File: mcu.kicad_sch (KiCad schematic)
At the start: 38 parts, among them Q4 MMBT3904, U2 AT32F403ACGT7, U3 QMI8658B, Y1 8MHz, Y2 32.768kHz

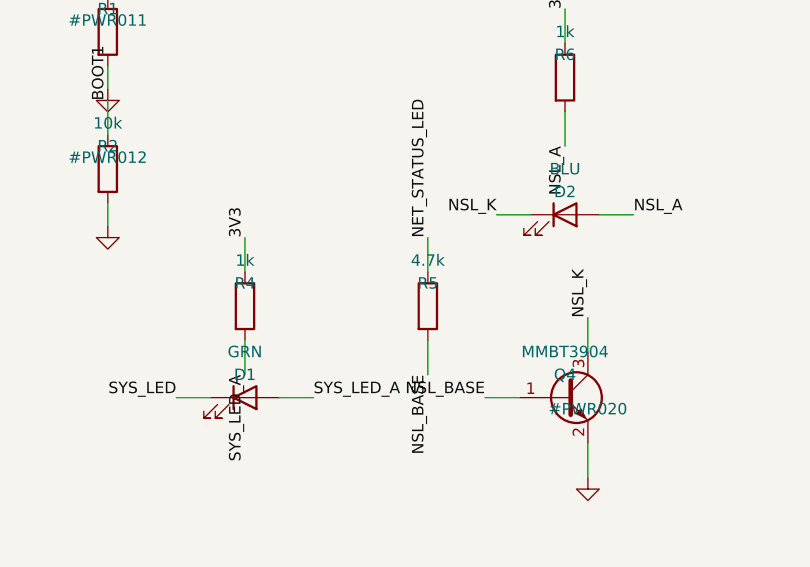
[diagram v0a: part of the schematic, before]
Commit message: M2: modem_rf ERC-clean (F-9 conditional release)
EC200U wired using ONLY Table-7-VERIFIED pins; all 76 NEEDS-HUMAN pins are
no-connect with F9-REVIEW text markers on the sheet. VBAT (57-60) via Q3
AO3401A high-side switch (DEFAULT ON, MODEM_PWR_EN high = power cut via
Q14 NPN + Q13 PNP); PWRKEY/RESET_N NPN open-collector stages; STATUS per
Quectel Fig 28 NPN stage (MODEM_STATUS INVERTED at MCU - firmware note);
UART/RI/DTR through TXB0104PWR (VccA=VDD_EXT 1.8V, OE held low until
VDD_EXT rises); USIM with 33R series + SMF05C + nano holder + MFF2 eSIM
pads DNP behind 0R selects; USB to 4 test pads via USBLC6-2SC6; NETLIGHT
NPN LED; pi networks (0R fitted, shunts DNP) to 2x XY-IPEX1 U.FL.

Root-sheet layout bug fixed: a 5th sheet wrapped onto column 0 and its
pin stubs shorted into the mcu sheet's stubs (5V0/ADC_SPARE, CAN1_RX/SYS,
CAN1_TX/VIN) - rows added. USIM_VDD 0R select was defeated by a label
bridge - holder now on USIM_VDD_SIM only.

Co-Authored-By: Claude Fable 5 <noreply@anthropic.com>
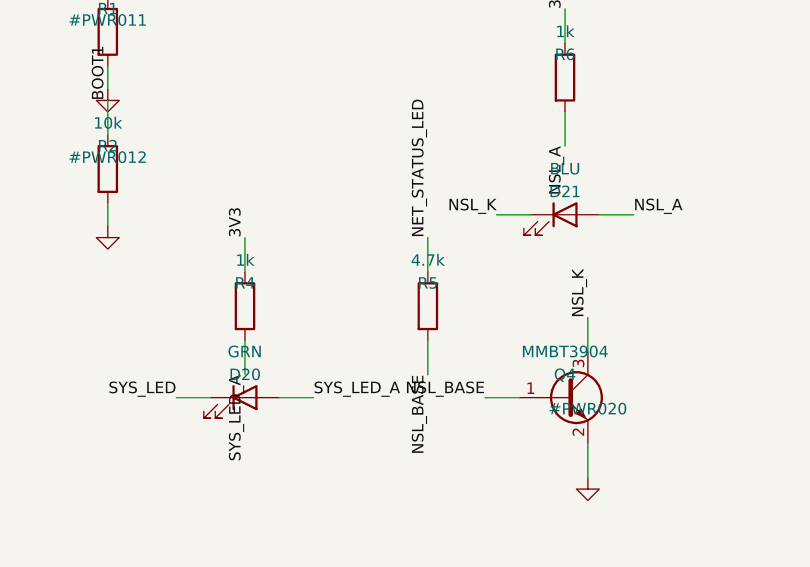
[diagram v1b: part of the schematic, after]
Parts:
- removed D1: GRN, LED_SMD:LED_0603_1608Metric, symbol Device:LED
- removed D2: BLU, LED_SMD:LED_0603_1608Metric, symbol Device:LED
- added D20: GRN, LED_SMD:LED_0603_1608Metric, symbol Device:LED
- added D21: BLU, LED_SMD:LED_0603_1608Metric, symbol Device:LED
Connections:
- net NSL_A: now also D21.2 (A)
- net NSL_K: now also D21.1 (K)
- net SYS_LED: now also D20.1 (K)
- net SYS_LED_A: now also D20.2 (A)
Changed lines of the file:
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@@
 		(dnp no)
 		(fields_autoplaced yes)
-		(property "Reference" "D1"
+		(property "Reference" "D20"
 			(at 320.04 198.12 0)
 			(effects
@@
 			(project "telematics-tracker"
 				(path "/784bc421-9fc7-43cb-bfc3-562714cb3f68/f6e9097b-45bc-5b1a-80f4-03a0e0f8043a"
-					(reference "D1")
+					(reference "D20")
 					(unit 1)
 				)
@@
 		(dnp no)
 		(fields_autoplaced yes)
-		(property "Reference" "D2"
+		(property "Reference" "D21"
 			(at 355.6 177.8 0)
 			(effects
@@
 			(project "telematics-tracker"
 				(path "/784bc421-9fc7-43cb-bfc3-562714cb3f68/f6e9097b-45bc-5b1a-80f4-03a0e0f8043a"
-					(reference "D2")
-					(unit 1)
-				)
+					(reference "D21")
+					(unit 1)
+				)

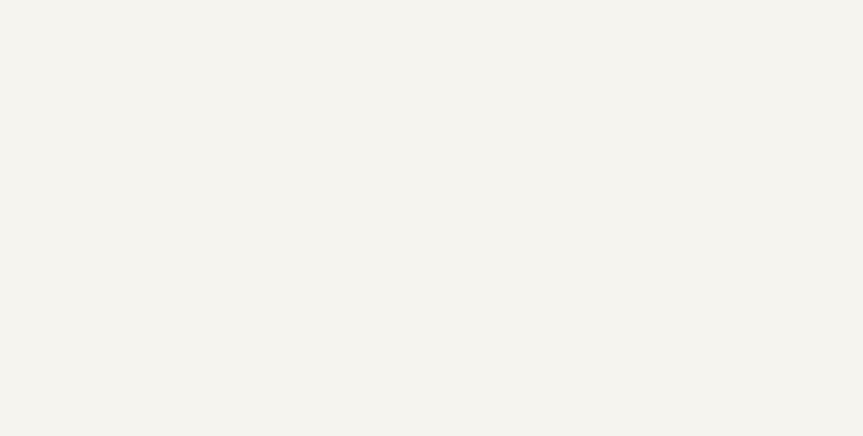
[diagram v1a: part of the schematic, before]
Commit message: M3 close: F-15 R80 1R, F-14 six test points, ambient rating, CPWG geometry
F-15: R80 10R (C3013385) -> 1R anti-surge FRS2512F1R00TS (C55348540).
At the 10.5 V floor and full load the 10R version had NO load-line solution:
V_B^2 - 9.8*V_B + 59 = 0, discriminant -140. Max power transfer through 10R
from 9.8 V is V^2/4R = 2.4 W against a 5.9 W demand - a hard brown-out. At 1R:
V_B = 9.16 V, I = 0.644 A, 0.41 W worst-case continuous, 24 W ceiling.
Pulse energy unchanged at 8.5 mJ (E = CdV^2/2 is independent of R) but peak
goes 384 W -> 3.8 kW and tau 44 us -> 4.4 us, which is why the part must be
anti-surge rather than plain thick film. Confirming that pulse curve joins F-12
on the bench list.

F-14: TP23 VIN, TP24 VBAT_MODEM, TP25 CANH, TP26 CANL, TP27 MODEM_TX,
TP28 MODEM_RX. Each verified against the netlist to share its net with the
real circuit nodes. hier() used for hierarchical nets and net() only for
sheet-local ones, so ERC stayed at exactly 0 errors / 14 warnings with no new
same_local_global_label entries. Rule 8 now MET (28 test points).

Product spec: rated operating ambient -20 to +70 C, housing shaded or
light-coloured, 85 C survival not operating - added to handoff section 1.1 and
a new docs/installation-sheet.md. Governed by U1: EC200U V1.2 Table 42 p.75
gives operating -35..+75 C (meets 3GPP) and extended -40..+85 C (functions
maintained but Pout may exceed 3GPP tolerances), so +70 C keeps 5 C to the
compliant limit and 85 C is exactly the extended limit.

NEW FLAG F-19: typical 1S Li-ion is -20..+60 C discharge, narrower than the
+70 C product ceiling. Charging is already protected by the BQ25606 JEITA
network; discharge above 60 C and calendar ageing are not. Decision needed -
accept with a shorter battery service interval, or narrow the rating to +60 C.

M4 input: 50 ohm CPWG for JLC7628 L1-L2 computed via Ghione-Naldi conformal
mapping (elliptic integrals by AGM), cross-checked against Hammerstad-Jensen
microstrip. h = 0.2104 mm (1x 7628 prepreg). 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
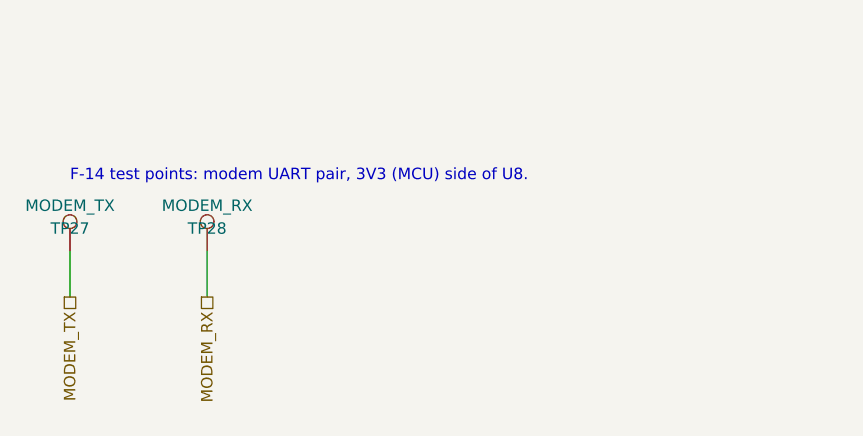
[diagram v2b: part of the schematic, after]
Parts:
- added TP27: MODEM_TX, TestPoint:TestPoint_Pad_D1.5mm, symbol Connector:TestPoint
- added TP28: MODEM_RX, TestPoint:TestPoint_Pad_D1.5mm, symbol Connector:TestPoint
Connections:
- net MODEM_RX: now also TP28.1
- net MODEM_TX: now also TP27.1
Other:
- note added: "F-14 test points: modem UART pair, 3V3 (MCU) side of U8."
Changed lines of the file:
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@@
 	(wire
 		(pts
+			(xy 30.48 271.78) (xy 30.48 276.86)
+		)
+		(stroke
+			(width 0)
+			(type default)
+		)
+	)
+	(hierarchical_label "MODEM_TX"
+		(shape passive)
+		(at 30.48 276.86 270)
+		(effects
+			(font
+				(size 1.27 1.27)
+			)
+			(justify right)
+		)
+	)
+	(wire
+		(pts
+			(xy 45.72 271.78) (xy 45.72 276.86)
+		)
+		(stroke
+			(width 0)
+			(type default)
+		)
+	)
+	(hierarchical_label "MODEM_RX"
+		(shape passive)
+		(at 45.72 276.86 270)
+		(effects
+			(font
+				(size 1.27 1.27)
+			)
+			(justify right)
+		)
+	)
+	(text "F-14 test points: modem UART pair, 3V3 (MCU) side of U8."
+		(exclude_from_sim no)
+		(at 30.48 264.16 0)
+		(effects
+			(font
+				(size 1.27 1.27)
+			)
+			(justify left bottom)
+		)
+	)
+	(wire
+		(pts
 			(xy 38.1 215.9) (xy 38.1 220.98)
 		)
@@
 					(unit 1)
 				)
+			)
+		)
+	)
+	(symbol
+		(lib_id "Connector:TestPoint")
+		(at 30.48 271.78 0)
+		(unit 1)
+		(exclude_from_sim no)
+		(in_bom yes)
+		(on_board yes)
+		(dnp no)
+		(fields_autoplaced yes)
+		(property "Reference" "TP27"
+			(at 30.48 269.24 0)
+			(effects
+				(font
+					(size 1.27 1.27)
+				)
+			)
+		)
+		(property "Value" "MODEM_TX"
+			(at 30.48 266.7 0)
+			(effects
+				(font
+					(size 1.27 1.27)
+				)
+			)
+		)
+		(property "Footprint" "TestPoint:TestPoint_Pad_D1.5mm"
+			(at 30.48 271.78 0)
+			(hide yes)
+			(effects
+				(font
+					(size 1.27 1.27)
+				)
+			)
+		)
+		(property "Datasheet" "~"
+			(at 30.48 271.78 0)
+			(hide yes)
+			(effects
+				(font
+					(size 1.27 1.27)
+				)
+			)
+		)
+		(pin "1"
+		)
+		(instances
+			(project "telematics-tracker"
+				(path "/784bc421-9fc7-43cb-bfc3-562714cb3f68/f6e9097b-45bc-5b1a-80f4-03a0e0f8043a"
+					(reference "TP27")
+					(unit 1)
+				)
+			)
+		)
+	)
+	(symbol
+		(lib_id "Connector:TestPoint")
+		(at 45.72 271.78 0)
+		(unit 1)
+		(exclude_from_sim no)
+		(in_bom yes)
+		(on_board yes)
+		(dnp no)
+		(fields_autoplaced yes)
+		(property "Reference" "TP28"
+			(at 45.72 269.24 0)
+			(effects
+				(font
+					(size 1.27 1.27)
+				)
+			)
+		)
+		(property "Value" "MODEM_RX"
+			(at 45.72 266.7 0)
+			(effects
+				(font
+					(size 1.27 1.27)
+				)
+			)
+		)
+		(property "Footprint" "TestPoint:TestPoint_Pad_D1.5mm"
+			(at 45.72 271.78 0)
+			(hide yes)
+			(effects
+				(font
+					(size 1.27 1.27)
+				)
+			)
+		)
+		(property "Datasheet" "~"
+			(at 45.72 271.78 0)
+			(hide yes)
+			(effects
+				(font
+					(size 1.27 1.27)
+				)
+			)
+		)
+		(pin "1"
+		)
+		(instances
+			(project "telematics-tracker"
+				(path "/784bc421-9fc7-43cb-bfc3-562714cb3f68/f6e9097b-45bc-5b1a-80f4-03a0e0f8043a"
+					(reference "TP28")
+					(unit 1)
+				)

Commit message: Step 1-3: fix rule floors, classify SW_BUCK as HV, shrink, fix HV router
Step 1 - rule mismatch fixed and verified:
  netclasses.py gains BOARD_RULES + _assert_floors(). Every class now meets
  track >= 0.20 mm and via annulus >= 0.10 mm. min_clearance had been silently
  reset to 0.0 by a KiCad round trip; restored to 0.15 and now asserted after
  the round trip so it cannot regress unnoticed. Exported DSN verified to carry
  the values (kicad_default 200, GND 500, MODEM_BULK 2000, RF 400, HV 500/600).

Step 2 - HV hand-routing, and three real defects it uncovered:

  1. /power/SW_BUCK was in the Default netclass. It is the buck switching node:
     it swings from GND to VIN every cycle, so it is a 100 V net with fast
     edges, and it was running at 0.20 mm track / 0.15 mm clearance. U5_VB
     (bootstrap) rides on it and was equally misclassified. Both moved to HV.
     Found because the maze router treated SW_BUCK as LV and threw a 1.50 mm
     halo around U5's own VIN pins, making /power/VIN_B unroutable at 0/4.

  2. HV_ZONE stopped at x = 20.0 and so EXCLUDED the buck primary side. U5 sits
     at x 35.4..42.3 with C73, C74 and D16 beside it, and VIN_B runs 22 mm from
     R80 to reach it. The highest-energy node on the board was outside the HV
     rule area - which also meant the U5 package exception approved under F-20
     was dead code, since it is conditioned on insideArea('HV_ZONE'). HV_ZONE
     is now L-shaped: left strip plus the buck primary.

  3. Three defects in pcbroute_hv.py itself, together responsible for 128 of
     the 129 clearance violations the first routed board had:
       - halos were sized for a 0.50 mm track (half 0.25) but the router also
         drops 0.80 mm vias, so cells legal for a track were illegal for a via
       - halo extents were quantised with round(), letting a cell centre sit up
         to RES/2 = 0.075 mm inside the forbidden region. That is exactly the
         size of the 0.545..0.594 mm shortfalls DRC reporte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
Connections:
- net ADC_SPARE: no longer names the net of U2.19 (PB1)
- no-connect marks 2 -> 3
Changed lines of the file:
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@@
-	(wire
-		(pts
-			(xy 168.91 166.37) (xy 158.75 166.37)
-		)
-		(stroke
-			(width 0)
-			(type default)
-		)
-	)
-	(hierarchical_label "ADC_SPARE"
-		(shape passive)
-		(at 158.75 166.37 180)
-		(effects
-			(font
-				(size 1.27 1.27)
-			)
-			(justify right)
-		)
-	)
 	(wire
 		(pts
@@
 		)
 	)
-	(wire
+	(no_connect
+		(at 168.91 166.37)
+	)
+	(wire

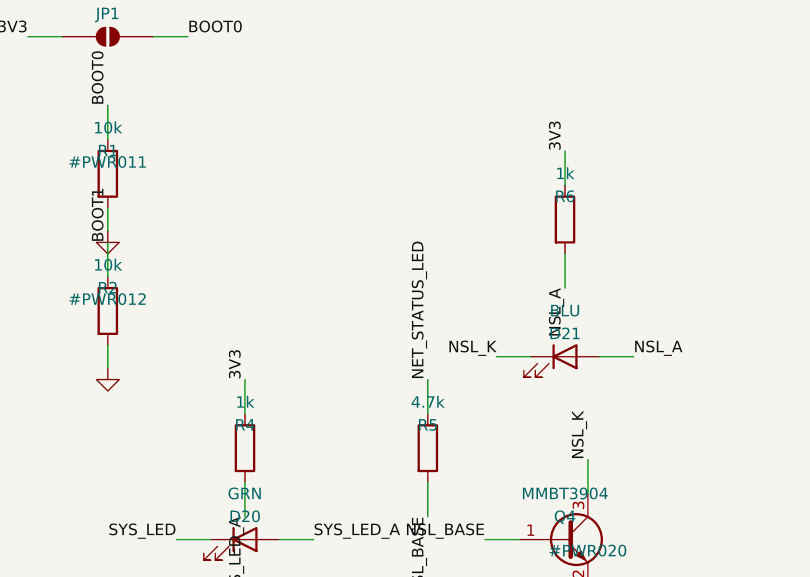
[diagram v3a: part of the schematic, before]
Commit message: BOM verification (milestone 5): 28 wrong or unverified lines fixed against LCSC/JLCPCB data; F-5 and F-22 closed
Wrong values (C1/C2 22pF for 18pF, C3/C4, R56/R58 10k for 47k, R66-R68
100R for 33R), wrong packages (C12/C63, C83, R71/R72, Y1 5032 on a 3225
footprint), Y2 12.5pF crystal on 6.8pF caps (now a 7pF FC-135), red LED
number on the green and blue LEDs (R4/R6 330R for their Vf), a
non-existent C-number (2.2k), and nine TBD placeholders.

tools/bom_audit.py: value / voltage / package / LED colour / crystal load /
stock (JLCPCB and LCSC) per line -> docs/bom-audit.md, out/bom-mpn.csv
(manufacturer + MPN). Netlist connectivity unchanged, ERC 0, checkpins ok.

Co-Authored-By: Claude Opus 5.5 <noreply@anthropic.com>
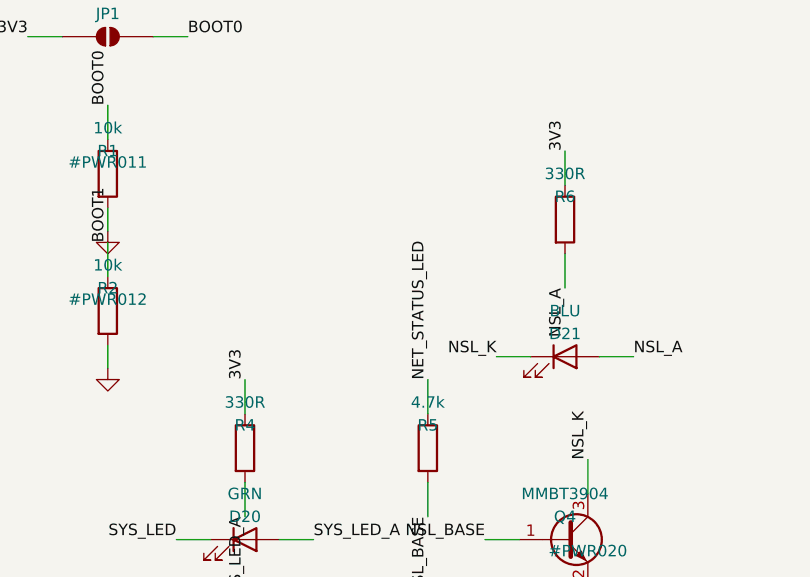
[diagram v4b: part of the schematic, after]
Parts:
- C1, C2: LCSC C1653 -> C1647
- C12: LCSC C23733 -> C1779
- C3, C4: LCSC C1555 -> C318672
- D20: LCSC C2286 -> C12624
- D21: LCSC C2286 -> C2288
- R4, R6: value 1k -> 330R; LCSC C17513 -> C17630
- R7, R8: LCSC C4356 -> C17520
- Y1: LCSC C115962 -> C2682775
- Y2: LCSC C32346 -> C48615
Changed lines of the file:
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@@
 			)
 		)
-		(property "LCSC" "C115962"
+		(property "LCSC" "C2682775"
 			(at 111.76 132.08 0)
 			(hide yes)
@@
 			)
 		)
-		(property "LCSC" "C1653"
+		(property "LCSC" "C1647"
 			(at 106.68 144.78 0)
 			(hide yes)
@@
 			)
 		)
-		(property "LCSC" "C1653"
+		(property "LCSC" "C1647"
 			(at 119.38 144.78 0)
 			(hide yes)
@@
 			)
 		)
-		(property "LCSC" "C32346"
+		(property "LCSC" "C48615"
 			(at 111.76 106.68 0)
 			(hide yes)
@@
 			)
 		)
-		(property "LCSC" "C1555"
+		(property "LCSC" "C318672"
 			(at 106.68 116.84 0)
 			(hide yes)
@@
 			)
 		)
-		(property "LCSC" "C1555"
+		(property "LCSC" "C318672"
 			(at 119.38 116.84 0)
 			(hide yes)
@@
 			)
 		)
-		(property "LCSC" "C23733"
+		(property "LCSC" "C1779"
 			(at 350.52 81.28 0)
 			(hide yes)
@@
 			)
 		)
-		(property "Value" "1k"
+		(property "Value" "330R"
 			(at 320.04 185.42 0)
 			(effects
@@
 			)
 		)
-		(property "LCSC" "C17513"
+		(property "LCSC" "C17630"
 			(at 320.04 190.5 0)
 			(hide yes)
@@
 			)
 		)
-		(property "LCSC" "C2286"
+		(property "LCSC" "C12624"
 			(at 320.04 200.66 0)
 			(hide yes)
@@
 			)
 		)
-		(property "LCSC" "C2286"
+		(property "LCSC" "C2288"
 			(at 355.6 180.34 0)
 			(hide yes)
@@
 			)
 		)
-		(property "Value" "1k"
+		(property "Value" "330R"
 			(at 355.6 160.02 0)
 			(effects
@@
 			)
 		)
-		(property "LCSC" "C17513"
+		(property "LCSC" "C17630"
 			(at 355.6 165.1 0)
 			(hide yes)
@@
 			)
 		)
-		(property "LCSC" "C4356"
+		(property "LCSC" "C17520"
 			(at 269.24 83.82 0)
 			(hide yes)
@@
 			)
 		)
-		(property "LCSC" "C4356"
+		(property "LCSC" "C17520"
 			(at 279.4 83.82 0)
 			(hide yes)

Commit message: Pre-order verification review: 12 would-fail faults fixed, report added
Schematic (tools/sheets.py, sheets regenerated):
- D2 SMDJ100A: D_Zener symbol, cathode to VIN_P (was drawn forward with
  the bidirectional D_TVS symbol)
- D10/D11 BAV99 clamps: pin 1 (anode) GND, pin 2 (cathode) 3V3 (KiCad's
  hidden K/A/K pin names contradict the Nexperia pinout)
- D5/D6: BAV70 common-cathode replaces the mirrored BAV99 (opto LED was
  bypassed)
- U8 TXB0104 OE: 10k/100k = 1.64 V (47k/10k gave 0.32 V, UART disabled)
- R82 0.1R: EG11752 2 A peak limit (0R disabled it)
- D7/D8 flyback cathodes to VIN_P behind D1 (reverse-polarity path via
  the Q1/Q2 body diodes), VIN_P exported as a hierarchical net
- Q1/Q2 gate pulldown 100k (4.89 V; 10k gave 4.07 V), DI pull-up 220k,
  R91 51k USIM_DET pull-up, PESD5V0L5UY SIM ESD, X7R 1uF/4.7uF, 100k
  C149504, comments and notes corrected

Board (DRC-gated routes via tools/manual_routes.py + tools/board_fixes.py):
- D2/D10/D11 turned, NRST via moved, VIN trunk re-laid around D7/D8,
  VIN_P B.Cu run to D1, R91 on B.Cu, VBAT_BT 0.6 mm F.Cu to J2, SW_CHG
  0.4 mm, PMID 0.3/0.5 mm, DNP flags, C61<->C80 swap, 28 RF stitching
  vias, 9 vias under U5's pad; values updated
- manual_routes: delvia/padnet/rotate/value/move ops, ACCEPT_EQUAL

Checks: parity 0 mismatches (212 parts, 727 pad nets), ERC 0 errors,
pin checklist pass, DRC 0 errors / 0 unconnected, BOM audit 76/76 clean.

Docs: firmware-notes FW-6/8/13/14/17 + FW-18..22, BV-1/5/6/7; handoff and
installation sheet corrected (12 V floor, DI not isolated, values);
design-log entry; docs/verification-report.pdf (OK / NOT OK per item).

Co-Authored-By: Claude Fable 5.1 <noreply@anthropic.com>
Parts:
- C12: LCSC C1779 -> C354262
- C14, C7: LCSC C15849 -> C106858
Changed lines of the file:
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@@
 			)
 		)
-		(property "LCSC" "C15849"
+		(property "LCSC" "C106858"
 			(at 83.82 106.68 0)
 			(hide yes)
@@
 			)
 		)
-		(property "LCSC" "C1779"
+		(property "LCSC" "C354262"
 			(at 350.52 81.28 0)
 			(hide yes)
@@
 			)
 		)
-		(property "LCSC" "C15849"
+		(property "LCSC" "C106858"
 			(at 259.08 76.2 0)
 			(hide yes)
